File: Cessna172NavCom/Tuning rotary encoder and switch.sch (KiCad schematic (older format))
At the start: 7 parts, among them SW3 Tuning encoder

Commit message: First full layout attempt, new 3D models
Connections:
- net labels added: A, B
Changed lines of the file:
@@
 $Descr A4 11693 8268
 encoding utf-8
-Sheet 7 8
+Sheet 5 8
 Title ""
 Date ""
@@
 AR Path="/5F5DD336/5F5D9322" Ref="SW4"  Part="1"
 AR Path="/5F5E0D77/5F5D9322" Ref="SW7"  Part="1"
-F 0 "SW7" H 6250 3650 50  0000 L CNN
+F 0 "SW3" H 6250 3650 50  0000 L CNN
 F 1 "Tuning encoder" H 6250 3750 50  0000 L CNN
 F 2 "Cessna 172 nav and com radio:EN11-HSM1BF20" H 5850 4110 50  0001 C CNN
@@
 AR Path="/5F5DD336/5F5D9328" Ref="R9"  Part="1"
 AR Path="/5F5E0D77/5F5D9328" Ref="R14"  Part="1"
-F 0 "R14" V 5043 3850 50  0000 C CNN
-F 1 "10k" V 5134 3850 50  0000 C CNN
+F 0 "R5" V 5450 3850 50  0000 C CNN
+F 1 "10k" V 5350 3850 50  0000 C CNN
 F 2 "Resistor_SMD:R_0805_2012Metric_Pad1.15x1.40mm_HandSolder" V 5180 3850 50  0001 C CNN
 F 3 "~" H 5250 3850 50  0001 C CNN
 	1    5250 3850
-	0    1    1    0
+	0    -1   -1   0
 $EndComp
 $Comp
@@
 AR Path="/5F5DD336/5F5D932E" Ref="R10"  Part="1"
 AR Path="/5F5E0D77/5F5D932E" Ref="R15"  Part="1"
-F 0 "R15" V 5350 4050 50  0000 C CNN
+F 0 "R6" V 5350 4050 50  0000 C CNN
 F 1 "10k" V 5450 4050 50  0000 C CNN
 F 2 "Resistor_SMD:R_0805_2012Metric_Pad1.15x1.40mm_HandSolder" V 5180 4050 50  0001 C CNN
@@
 AR Path="/5F5DD336/5F5D9337" Ref="C9"  Part="1"
 AR Path="/5F5E0D77/5F5D9337" Ref="C11"  Part="1"
-F 0 "C11" V 6150 4400 50  0000 C CNN
+F 0 "C7" V 6150 4400 50  0000 C CNN
 F 1 "0.1uf" V 5850 4400 50  0000 C CNN
 F 2 "Capacitor_SMD:C_0805_2012Metric_Pad1.15x1.40mm_HandSolder" H 6038 4250 50  0001 C CNN
@@
 AR Path="/5F5DD336/5F5D933D" Ref="C8"  Part="1"
 AR Path="/5F5E0D77/5F5D933D" Ref="C10"  Part="1"
-F 0 "C10" V 5850 3450 50  0000 L CNN
+F 0 "C6" V 5850 3450 50  0000 L CNN
 F 1 "0.1uf" V 6150 3400 50  0000 L CNN
 F 2 "Capacitor_SMD:C_0805_2012Metric_Pad1.15x1.40mm_HandSolder" H 6038 3350 50  0001 C CNN
@@
 AR Path="/5F5DD336/5F5D934C" Ref="R12"  Part="1"
 AR Path="/5F5E0D77/5F5D934C" Ref="R17"  Part="1"
-F 0 "R17" H 5670 4696 50  0000 L CNN
+F 0 "R8" H 5670 4696 50  0000 L CNN
 F 1 "10k" H 5670 4605 50  0000 L CNN
 F 2 "Resistor_SMD:R_0805_2012Metric_Pad1.15x1.40mm_HandSolder" V 5530 4650 50  0001 C CNN
@@
 AR Path="/5F5DD336/5F5D935D" Ref="R11"  Part="1"
 AR Path="/5F5E0D77/5F5D935D" Ref="R16"  Part="1"
-F 0 "R16" H 5670 3296 50  0000 L CNN
+F 0 "R7" H 5670 3296 50  0000 L CNN
 F 1 "10k" H 5670 3205 50  0000 L CNN
 F 2 "Resistor_SMD:R_0805_2012Metric_Pad1.15x1.40mm_HandSolder" V 5530 3250 50  0001 C CNN
@@
 	5600 3400 5600 3500
 Connection ~ 5600 3500
+Text HLabel 5600 3100 1    50   Output ~ 0
+LEFT
 Text HLabel 5600 4800 3    50   Output ~ 0
-LEFT
-Text HLabel 5600 3100 1    50   Output ~ 0
 RIGHT
 Text HLabel 6300 3850 2    50   Output ~ 0
 SW
+Text Label 5700 3500 0    50   ~ 0
+A
+Text Label 5700 4400 0    50   ~ 0
+B
 $EndSCHEMATC

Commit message: Re-work to use 5 digit LEDs
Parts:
- renumbered SW3 to SW4
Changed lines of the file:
@@
 $Descr A4 11693 8268
 encoding utf-8
-Sheet 5 8
+Sheet 7 8
 Title ""
 Date ""
@@
 P 6000 3950
 AR Path="/5F5D9322" Ref="SW?"  Part="1"
-AR Path="/5F5D6B2B/5F5D9322" Ref="SW3"  Part="1"
-AR Path="/5F5DD336/5F5D9322" Ref="SW4"  Part="1"
-AR Path="/5F5E0D77/5F5D9322" Ref="SW7"  Part="1"
-F 0 "SW3" H 6250 3650 50  0000 L CNN
+AR Path="/5F5D6B2B/5F5D9322" Ref="SW4"  Part="1"
+AR Path="/5F5DD336/5F5D9322" Ref="SW5"  Part="1"
+AR Path="/5F5E0D77/5F5D9322" Ref="SW6"  Part="1"
+F 0 "SW6" H 6250 3650 50  0000 L CNN
 F 1 "Tuning encoder" H 6250 3750 50  0000 L CNN
 F 2 "Cessna 172 nav and com radio:EN11-HSM1BF20" H 5850 4110 50  0001 C CNN
@@
 AR Path="/5F5D6B2B/5F5D9328" Ref="R5"  Part="1"
 AR Path="/5F5DD336/5F5D9328" Ref="R9"  Part="1"
-AR Path="/5F5E0D77/5F5D9328" Ref="R14"  Part="1"
-F 0 "R5" V 5450 3850 50  0000 C CNN
+AR Path="/5F5E0D77/5F5D9328" Ref="R13"  Part="1"
+F 0 "R13" V 5450 3850 50  0000 C CNN
 F 1 "10k" V 5350 3850 50  0000 C CNN
 F 2 "Resistor_SMD:R_0805_2012Metric_Pad1.15x1.40mm_HandSolder" V 5180 3850 50  0001 C CNN
@@
 AR Path="/5F5D6B2B/5F5D932E" Ref="R6"  Part="1"
 AR Path="/5F5DD336/5F5D932E" Ref="R10"  Part="1"
-AR Path="/5F5E0D77/5F5D932E" Ref="R15"  Part="1"
-F 0 "R6" V 5350 4050 50  0000 C CNN
+AR Path="/5F5E0D77/5F5D932E" Ref="R14"  Part="1"
+F 0 "R14" V 5350 4050 50  0000 C CNN
 F 1 "10k" V 5450 4050 50  0000 C CNN
 F 2 "Resistor_SMD:R_0805_2012Metric_Pad1.15x1.40mm_HandSolder" V 5180 4050 50  0001 C CNN
@@
 AR Path="/5F5DD336/5F5D9337" Ref="C9"  Part="1"
 AR Path="/5F5E0D77/5F5D9337" Ref="C11"  Part="1"
-F 0 "C7" V 6150 4400 50  0000 C CNN
+F 0 "C11" V 6150 4400 50  0000 C CNN
 F 1 "0.1uf" V 5850 4400 50  0000 C CNN
 F 2 "Capacitor_SMD:C_0805_2012Metric_Pad1.15x1.40mm_HandSolder" H 6038 4250 50  0001 C CNN
@@
 AR Path="/5F5DD336/5F5D933D" Ref="C8"  Part="1"
 AR Path="/5F5E0D77/5F5D933D" Ref="C10"  Part="1"
-F 0 "C6" V 5850 3450 50  0000 L CNN
+F 0 "C10" V 5850 3450 50  0000 L CNN
 F 1 "0.1uf" V 6150 3400 50  0000 L CNN
 F 2 "Capacitor_SMD:C_0805_2012Metric_Pad1.15x1.40mm_HandSolder" H 6038 3350 50  0001 C CNN
@@
 AR Path="/5F5D6B2B/5F5D934C" Ref="R8"  Part="1"
 AR Path="/5F5DD336/5F5D934C" Ref="R12"  Part="1"
-AR Path="/5F5E0D77/5F5D934C" Ref="R17"  Part="1"
-F 0 "R8" H 5670 4696 50  0000 L CNN
+AR Path="/5F5E0D77/5F5D934C" Ref="R16"  Part="1"
+F 0 "R16" H 5670 4696 50  0000 L CNN
 F 1 "10k" H 5670 4605 50  0000 L CNN
 F 2 "Resistor_SMD:R_0805_2012Metric_Pad1.15x1.40mm_HandSolder" V 5530 4650 50  0001 C CNN
@@
 AR Path="/5F5D6B2B/5F5D935D" Ref="R7"  Part="1"
 AR Path="/5F5DD336/5F5D935D" Ref="R11"  Part="1"
-AR Path="/5F5E0D77/5F5D935D" Ref="R16"  Part="1"
-F 0 "R7" H 5670 3296 50  0000 L CNN
+AR Path="/5F5E0D77/5F5D935D" Ref="R15"  Part="1"
+F 0 "R15" H 5670 3296 50  0000 L CNN
 F 1 "10k" H 5670 3205 50  0000 L CNN
 F 2 "Resistor_SMD:R_0805_2012Metric_Pad1.15x1.40mm_HandSolder" V 5530 3250 50  0001 C CNN

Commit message: New board size!
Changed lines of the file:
@@
 $Descr A4 11693 8268
 encoding utf-8
-Sheet 7 8
+Sheet 5 8
 Title ""
 Date ""
@@
 AR Path="/5F5DD336/5F5D9322" Ref="SW5"  Part="1"
 AR Path="/5F5E0D77/5F5D9322" Ref="SW6"  Part="1"
-F 0 "SW6" H 6250 3650 50  0000 L CNN
+F 0 "SW4" H 6250 3650 50  0000 L CNN
 F 1 "Tuning encoder" H 6250 3750 50  0000 L CNN
 F 2 "Cessna 172 nav and com radio:EN11-HSM1BF20" H 5850 4110 50  0001 C CNN
@@
 AR Path="/5F5DD336/5F5D9328" Ref="R9"  Part="1"
 AR Path="/5F5E0D77/5F5D9328" Ref="R13"  Part="1"
-F 0 "R13" V 5450 3850 50  0000 C CNN
+F 0 "R5" V 5450 3850 50  0000 C CNN
 F 1 "10k" V 5350 3850 50  0000 C CNN
 F 2 "Resistor_SMD:R_0805_2012Metric_Pad1.15x1.40mm_HandSolder" V 5180 3850 50  0001 C CNN
@@
 AR Path="/5F5DD336/5F5D932E" Ref="R10"  Part="1"
 AR Path="/5F5E0D77/5F5D932E" Ref="R14"  Part="1"
-F 0 "R14" V 5350 4050 50  0000 C CNN
+F 0 "R6" V 5350 4050 50  0000 C CNN
 F 1 "10k" V 5450 4050 50  0000 C CNN
 F 2 "Resistor_SMD:R_0805_2012Metric_Pad1.15x1.40mm_HandSolder" V 5180 4050 50  0001 C CNN
@@
 AR Path="/5F5DD336/5F5D9337" Ref="C9"  Part="1"
 AR Path="/5F5E0D77/5F5D9337" Ref="C11"  Part="1"
-F 0 "C11" V 6150 4400 50  0000 C CNN
+F 0 "C7" V 6150 4400 50  0000 C CNN
 F 1 "0.1uf" V 5850 4400 50  0000 C CNN
 F 2 "Capacitor_SMD:C_0805_2012Metric_Pad1.15x1.40mm_HandSolder" H 6038 4250 50  0001 C CNN
@@
 AR Path="/5F5DD336/5F5D933D" Ref="C8"  Part="1"
 AR Path="/5F5E0D77/5F5D933D" Ref="C10"  Part="1"
-F 0 "C10" V 5850 3450 50  0000 L CNN
+F 0 "C6" V 5850 3450 50  0000 L CNN
 F 1 "0.1uf" V 6150 3400 50  0000 L CNN
 F 2 "Capacitor_SMD:C_0805_2012Metric_Pad1.15x1.40mm_HandSolder" H 6038 3350 50  0001 C CNN
@@
 AR Path="/5F5DD336/5F5D934C" Ref="R12"  Part="1"
 AR Path="/5F5E0D77/5F5D934C" Ref="R16"  Part="1"
-F 0 "R16" H 5670 4696 50  0000 L CNN
+F 0 "R8" H 5670 4696 50  0000 L CNN
 F 1 "10k" H 5670 4605 50  0000 L CNN
 F 2 "Resistor_SMD:R_0805_2012Metric_Pad1.15x1.40mm_HandSolder" V 5530 4650 50  0001 C CNN
@@
 AR Path="/5F5DD336/5F5D935D" Ref="R11"  Part="1"
 AR Path="/5F5E0D77/5F5D935D" Ref="R15"  Part="1"
-F 0 "R15" H 5670 3296 50  0000 L CNN
+F 0 "R7" H 5670 3296 50  0000 L CNN
 F 1 "10k" H 5670 3205 50  0000 L CNN
 F 2 "Resistor_SMD:R_0805_2012Metric_Pad1.15x1.40mm_HandSolder" V 5530 3250 50  0001 C CNN

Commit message: Switch to USB for power, all parts on board
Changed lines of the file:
@@
 AR Path="/5F5DD336/5F5D9322" Ref="SW5"  Part="1"
 AR Path="/5F5E0D77/5F5D9322" Ref="SW6"  Part="1"
-F 0 "SW4" H 6250 3650 50  0000 L CNN
+F 0 "SW6" H 6250 3650 50  0000 L CNN
 F 1 "Tuning encoder" H 6250 3750 50  0000 L CNN
 F 2 "Cessna 172 nav and com radio:EN11-HSM1BF20" H 5850 4110 50  0001 C CNN
@@
 AR Path="/5F5DD336/5F5D9328" Ref="R9"  Part="1"
 AR Path="/5F5E0D77/5F5D9328" Ref="R13"  Part="1"
-F 0 "R5" V 5450 3850 50  0000 C CNN
+F 0 "R13" V 5450 3850 50  0000 C CNN
 F 1 "10k" V 5350 3850 50  0000 C CNN
 F 2 "Resistor_SMD:R_0805_2012Metric_Pad1.15x1.40mm_HandSolder" V 5180 3850 50  0001 C CNN
@@
 AR Path="/5F5DD336/5F5D932E" Ref="R10"  Part="1"
 AR Path="/5F5E0D77/5F5D932E" Ref="R14"  Part="1"
-F 0 "R6" V 5350 4050 50  0000 C CNN
+F 0 "R14" V 5350 4050 50  0000 C CNN
 F 1 "10k" V 5450 4050 50  0000 C CNN
 F 2 "Resistor_SMD:R_0805_2012Metric_Pad1.15x1.40mm_HandSolder" V 5180 4050 50  0001 C CNN
@@
 AR Path="/5F5DD336/5F5D9337" Ref="C9"  Part="1"
 AR Path="/5F5E0D77/5F5D9337" Ref="C11"  Part="1"
-F 0 "C7" V 6150 4400 50  0000 C CNN
+F 0 "C11" V 6150 4400 50  0000 C CNN
 F 1 "0.1uf" V 5850 4400 50  0000 C CNN
 F 2 "Capacitor_SMD:C_0805_2012Metric_Pad1.15x1.40mm_HandSolder" H 6038 4250 50  0001 C CNN
@@
 AR Path="/5F5DD336/5F5D933D" Ref="C8"  Part="1"
 AR Path="/5F5E0D77/5F5D933D" Ref="C10"  Part="1"
-F 0 "C6" V 5850 3450 50  0000 L CNN
+F 0 "C10" V 5850 3450 50  0000 L CNN
 F 1 "0.1uf" V 6150 3400 50  0000 L CNN
 F 2 "Capacitor_SMD:C_0805_2012Metric_Pad1.15x1.40mm_HandSolder" H 6038 3350 50  0001 C CNN
@@
 AR Path="/5F5DD336/5F5D934C" Ref="R12"  Part="1"
 AR Path="/5F5E0D77/5F5D934C" Ref="R16"  Part="1"
-F 0 "R8" H 5670 4696 50  0000 L CNN
+F 0 "R16" H 5670 4696 50  0000 L CNN
 F 1 "10k" H 5670 4605 50  0000 L CNN
 F 2 "Resistor_SMD:R_0805_2012Metric_Pad1.15x1.40mm_HandSolder" V 5530 4650 50  0001 C CNN
@@
 AR Path="/5F5DD336/5F5D935D" Ref="R11"  Part="1"
 AR Path="/5F5E0D77/5F5D935D" Ref="R15"  Part="1"
-F 0 "R7" H 5670 3296 50  0000 L CNN
+F 0 "R15" H 5670 3296 50  0000 L CNN
 F 1 "10k" H 5670 3205 50  0000 L CNN
 F 2 "Resistor_SMD:R_0805_2012Metric_Pad1.15x1.40mm_HandSolder" V 5530 3250 50  0001 C CNN

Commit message: Updated rotary encoder with proper footprint
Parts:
- removed SW4: Tuning encoder, Cessna 172 nav and com radio:EN11-HSM1BF20, symbol Device:Rotary_Encoder_Switch
- added J3: EN11-HSM1BF20, SamacSys_Parts:EN11HSM1BF20, symbol SamacSys_Parts:EN11-HSM1BF20
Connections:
- net labels added: A1, B1
- net labels removed: A, B
- no-connect marks 0 -> 2
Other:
- moved on the sheet: C10, C11, R15, R16
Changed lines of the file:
@@
 $Descr A4 11693 8268
 encoding utf-8
-Sheet 5 8
+Sheet 7 8
 Title ""
 Date ""
@@
 Comment4 ""
 $EndDescr
-$Comp
-L Device:Rotary_Encoder_Switch SW?
-U 1 1 5F5D9322
-P 6000 3950
-AR Path="/5F5D9322" Ref="SW?"  Part="1"
-AR Path="/5F5D6B2B/5F5D9322" Ref="SW4"  Part="1"
-AR Path="/5F5DD336/5F5D9322" Ref="SW5"  Part="1"
-AR Path="/5F5E0D77/5F5D9322" Ref="SW6"  Part="1"
-F 0 "SW6" H 6250 3650 50  0000 L CNN
-F 1 "Tuning encoder" H 6250 3750 50  0000 L CNN
-F 2 "Cessna 172 nav and com radio:EN11-HSM1BF20" H 5850 4110 50  0001 C CNN
-F 3 "~" H 6000 4210 50  0001 C CNN
-	1    6000 3950
-	1    0    0    -1
-$EndComp
 $Comp
 L Device:R R?
@@
 Text GLabel 5700 3950 0    50   Input ~ 0
 GND
-Text GLabel 6300 4050 2    50   Input ~ 0
+Text GLabel 6700 3950 2    50   Input ~ 0
 GND
 $Comp
 L Device:C C?
 U 1 1 5F5D9337
-P 6000 4400
+P 6000 4750
 AR Path="/5F5D9337" Ref="C?"  Part="1"
 AR Path="/5F5D6B2B/5F5D9337" Ref="C7"  Part="1"
 AR Path="/5F5DD336/5F5D9337" Ref="C9"  Part="1"
 AR Path="/5F5E0D77/5F5D9337" Ref="C11"  Part="1"
-F 0 "C11" V 6150 4400 50  0000 C CNN
-F 1 "0.1uf" V 5850 4400 50  0000 C CNN
-F 2 "Capacitor_SMD:C_0805_2012Metric_Pad1.15x1.40mm_HandSolder" H 6038 4250 50  0001 C CNN
-F 3 "~" H 6000 4400 50  0001 C CNN
-	1    6000 4400
+F 0 "C11" V 6150 4750 50  0000 C CNN
+F 1 "0.1uf" V 5850 4750 50  0000 C CNN
+F 2 "Capacitor_SMD:C_0805_2012Metric_Pad1.15x1.40mm_HandSolder" H 6038 4600 50  0001 C CNN
+F 3 "~" H 6000 4750 50  0001 C CNN
+	1    6000 4750
 	0    -1   -1   0
 $EndComp
@@
 L Device:C C?
 U 1 1 5F5D933D
-P 6000 3500
+P 6000 3100
 AR Path="/5F5D933D" Ref="C?"  Part="1"
 AR Path="/5F5D6B2B/5F5D933D" Ref="C6"  Part="1"
 AR Path="/5F5DD336/5F5D933D" Ref="C8"  Part="1"
 AR Path="/5F5E0D77/5F5D933D" Ref="C10"  Part="1"
-F 0 "C10" V 5850 3450 50  0000 L CNN
-F 1 "0.1uf" V 6150 3400 50  0000 L CNN
-F 2 "Capacitor_SMD:C_0805_2012Metric_Pad1.15x1.40mm_HandSolder" H 6038 3350 50  0001 C CNN
-F 3 "~" H 6000 3500 50  0001 C CNN
-	1    6000 3500
+F 0 "C10" V 5850 3050 50  0000 L CNN
+F 1 "0.1uf" V 6150 3000 50  0000 L CNN
+F 2 "Capacitor_SMD:C_0805_2012Metric_Pad1.15x1.40mm_HandSolder" H 6038 2950 50  0001 C CNN
+F 3 "~" H 6000 3100 50  0001 C CNN
+	1    6000 3100
 	0    1    1    0
 $EndComp
-Text GLabel 6150 4400 2    50   Input ~ 0
+Text GLabel 6150 4750 2    50   Input ~ 0
 GND
-Text GLabel 6150 3500 2    50   Input ~ 0
+Text GLabel 6150 3100 2    50   Input ~ 0
 GND
 Wire Wire Line
@@
 L Device:R R?
 U 1 1 5F5D934C
-P 5600 4650
+P 5600 5000
 AR Path="/5F5D934C" Ref="R?"  Part="1"
 AR Path="/5F5D6B2B/5F5D934C" Ref="R8"  Part="1"
 AR Path="/5F5DD336/5F5D934C" Ref="R12"  Part="1"
 AR Path="/5F5E0D77/5F5D934C" Ref="R16"  Part="1"
-F 0 "R16" H 5670 4696 50  0000 L CNN
-F 1 "10k" H 5670 4605 50  0000 L CNN
-F 2 "Resistor_SMD:R_0805_2012Metric_Pad1.15x1.40mm_HandSolder" V 5530 4650 50  0001 C CNN
-F 3 "~" H 5600 4650 50  0001 C CNN
-	1    5600 4650
+F 0 "R16" H 5670 5046 50  0000 L CNN
+F 1 "10k" H 5670 4955 50  0000 L CNN
+F 2 "Resistor_SMD:R_0805_2012Metric_Pad1.15x1.40mm_HandSolder" V 5530 5000 50  0001 C CNN
+F 3 "~" H 5600 5000 50  0001 C CNN
+	1    5600 5000
 	1    0    0    -1
 $EndComp
-Wire Wire Line
-	5600 4500 5600 4400
 Connection ~ 5600 4050
 Wire Wire Line
 	5600 4050 5700 4050
-Wire Wire Line
-	5850 4400 5600 4400
-Connection ~ 5600 4400
-Wire Wire Line
-	5600 4400 5600 4050
-Wire Wire Line
-	5600 3850 5600 3500
-Wire Wire Line
-	5600 3500 5850 3500
 Connection ~ 5600 3850
 Wire Wire Line
@@
 L Device:R R?
 U 1 1 5F5D935D
-P 5600 3250
+P 5600 2850
 AR Path="/5F5D935D" Ref="R?"  Part="1"
 AR Path="/5F5D6B2B/5F5D935D" Ref="R7"  Part="1"
 AR Path="/5F5DD336/5F5D935D" Ref="R11"  Part="1"
 AR Path="/5F5E0D77/5F5D935D" Ref="R15"  Part="1"
-F 0 "R15" H 5670 3296 50  0000 L CNN
-F 1 "10k" H 5670 3205 50  0000 L CNN
-F 2 "Resistor_SMD:R_0805_2012Metric_Pad1.15x1.40mm_HandSolder" V 5530 3250 50  0001 C CNN
-F 3 "~" H 5600 3250 50  0001 C CNN
-	1    5600 3250
+F 0 "R15" H 5670 2896 50  0000 L CNN
+F 1 "10k" H 5670 2805 50  0000 L CNN
+F 2 "Resistor_SMD:R_0805_2012Metric_Pad1.15x1.40mm_HandSolder" V 5530 2850 50  0001 C CNN
+F 3 "~" H 5600 2850 50  0001 C CNN
+	1    5600 2850
 	1    0    0    -1
 $EndComp
+Text HLabel 5600 2700 1    50   Output ~ 0
+LEFT
+Text HLabel 5600 5150 3    50   Output ~ 0
+RIGHT
+Text HLabel 6700 3850 2    50   Output ~ 0
+SW
+$Comp
+L SamacSys_Parts:EN11-HSM1BF20 J3
+U 1 1 5F66C873
+P 6200 3450
+AR Path="/5F5D6B2B/5F66C873" Ref="J3"  Part="1"
+AR Path="/5F5DD336/5F66C873" Ref="J4"  Part="1"
+AR Path="/5F5E0D77/5F66C873" Ref="J5"  Part="1"
+F 0 "J5" V 6019 3450 50  0000 C CNN
+F 1 "EN11-HSM1BF20" V 6110 3450 50  0000 C CNN
+F 2 "SamacSys_Parts:EN11HSM1BF20" H 7050 3750 50  0001 L CNN
+F 3 "" H 7050 3650 50  0001 L CNN
+F 4 "Mechanical Encoder Rotary Incremental Flat 0.018N.m Straight Gray Digital Square Wave 20PPR Through Hole PC Pin" H 7050 3550 50  0001 L CNN "Description"
+F 5 "26.2" H 7050 3450 50  0001 L CNN "Height"
+F 6 "858-EN11-HSM1BF20" H 7050 3350 50  0001 L CNN "Mouser Part Number"
+F 7 "https://www.mouser.co.uk/ProductDetail/BI-Technologies-TT-Electronics/EN11-HSM1BF20?qs=%252BUYXD5bnyXp4Uf1MU7v3zw%3D%3D" H 7050 3250 50  0001 L CNN "Mouser Price/Stock"
+F 8 "BI Technologies" H 7050 3150 50  0001 L CNN "Manufacturer_Name"
+F 9 "EN11-HSM1BF20" H 7050 3050 50  0001 L CNN "Manufacturer_Part_Number"
+	1    6200 3450
+	0    1    1    0
+$EndComp
 Wire Wire Line
-	5600 3400 5600 3500
-Connection ~ 5600 3500
-Text HLabel 5600 3100 1    50   Output ~ 0
-LEFT
-Text HLabel 5600 4800 3    50   Output ~ 0
-RIGHT
-Text HLabel 6300 3850 2    50   Output ~ 0
-SW
-Text Label 5700 3500 0    50   ~ 0
-A
-Text Label 5700 4400 0    50   ~ 0
-B
+	5600 3000 5600 3100
+Wire Wire Line
+	5600 3100 5850 3100
+Connection ~ 5600 3100
+Wire Wire Line
+	5600 3100 5600 3850
+NoConn ~ 6200 3450
+NoConn ~ 6200 4450
+Wire Wire Line
+	5600 4750 5850 4750
+Wire Wire Line
+	5600 4050 5600 4750
+Wire Wire Line
+	5600 4750 5600 4850
+Connection ~ 5600 4750
+Text Label 5700 4750 0    50   ~ 0
+B1
+Text Label 5700 3100 0    50   ~ 0
+A1
 $EndSCHEMATC

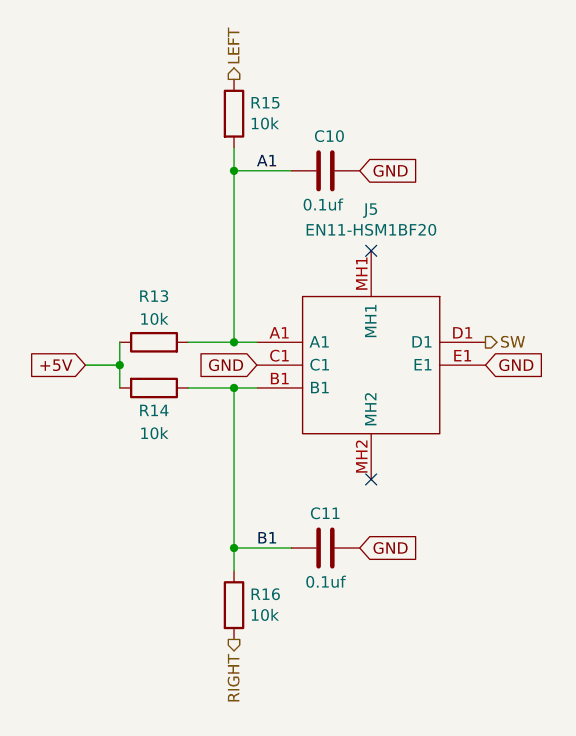
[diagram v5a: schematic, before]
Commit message: Connection, footprint, and layout updates
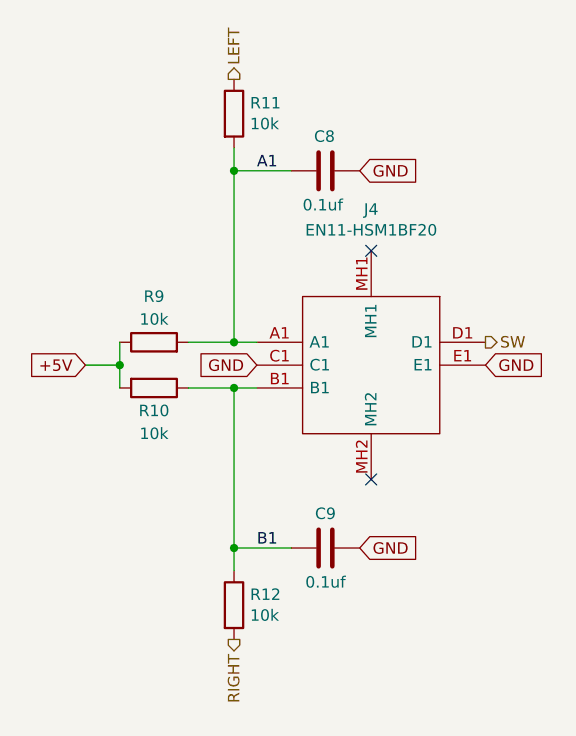
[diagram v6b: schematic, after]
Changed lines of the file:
@@
 $Descr A4 11693 8268
 encoding utf-8
-Sheet 7 8
+Sheet 6 8
 Title ""
 Date ""
@@
 AR Path="/5F5DD336/5F5D9328" Ref="R9"  Part="1"
 AR Path="/5F5E0D77/5F5D9328" Ref="R13"  Part="1"
-F 0 "R13" V 5450 3850 50  0000 C CNN
+F 0 "R9" V 5450 3850 50  0000 C CNN
 F 1 "10k" V 5350 3850 50  0000 C CNN
 F 2 "Resistor_SMD:R_0805_2012Metric_Pad1.15x1.40mm_HandSolder" V 5180 3850 50  0001 C CNN
@@
 AR Path="/5F5DD336/5F5D932E" Ref="R10"  Part="1"
 AR Path="/5F5E0D77/5F5D932E" Ref="R14"  Part="1"
-F 0 "R14" V 5350 4050 50  0000 C CNN
+F 0 "R10" V 5350 4050 50  0000 C CNN
 F 1 "10k" V 5450 4050 50  0000 C CNN
 F 2 "Resistor_SMD:R_0805_2012Metric_Pad1.15x1.40mm_HandSolder" V 5180 4050 50  0001 C CNN
@@
 AR Path="/5F5DD336/5F5D9337" Ref="C9"  Part="1"
 AR Path="/5F5E0D77/5F5D9337" Ref="C11"  Part="1"
-F 0 "C11" V 6150 4750 50  0000 C CNN
+F 0 "C9" V 6150 4750 50  0000 C CNN
 F 1 "0.1uf" V 5850 4750 50  0000 C CNN
 F 2 "Capacitor_SMD:C_0805_2012Metric_Pad1.15x1.40mm_HandSolder" H 6038 4600 50  0001 C CNN
@@
 AR Path="/5F5DD336/5F5D933D" Ref="C8"  Part="1"
 AR Path="/5F5E0D77/5F5D933D" Ref="C10"  Part="1"
-F 0 "C10" V 5850 3050 50  0000 L CNN
+F 0 "C8" V 5850 3050 50  0000 L CNN
 F 1 "0.1uf" V 6150 3000 50  0000 L CNN
 F 2 "Capacitor_SMD:C_0805_2012Metric_Pad1.15x1.40mm_HandSolder" H 6038 2950 50  0001 C CNN
@@
 AR Path="/5F5DD336/5F5D934C" Ref="R12"  Part="1"
 AR Path="/5F5E0D77/5F5D934C" Ref="R16"  Part="1"
-F 0 "R16" H 5670 5046 50  0000 L CNN
+F 0 "R12" H 5670 5046 50  0000 L CNN
 F 1 "10k" H 5670 4955 50  0000 L CNN
 F 2 "Resistor_SMD:R_0805_2012Metric_Pad1.15x1.40mm_HandSolder" V 5530 5000 50  0001 C CNN
@@
 AR Path="/5F5DD336/5F5D935D" Ref="R11"  Part="1"
 AR Path="/5F5E0D77/5F5D935D" Ref="R15"  Part="1"
-F 0 "R15" H 5670 2896 50  0000 L CNN
+F 0 "R11" H 5670 2896 50  0000 L CNN
 F 1 "10k" H 5670 2805 50  0000 L CNN
 F 2 "Resistor_SMD:R_0805_2012Metric_Pad1.15x1.40mm_HandSolder" V 5530 2850 50  0001 C CNN
@@
 AR Path="/5F5DD336/5F66C873" Ref="J4"  Part="1"
 AR Path="/5F5E0D77/5F66C873" Ref="J5"  Part="1"
-F 0 "J5" V 6019 3450 50  0000 C CNN
+F 0 "J4" V 6019 3450 50  0000 C CNN
 F 1 "EN11-HSM1BF20" V 6110 3450 50  0000 C CNN
 F 2 "SamacSys_Parts:EN11HSM1BF20" H 7050 3750 50  0001 L CNN
